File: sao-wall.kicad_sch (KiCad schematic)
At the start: 28 parts, among them J1 Conn_02x03_Odd_Even, J2 Conn_02x03_Odd_Even, J3 Conn_02x03_Odd_Even, J4 Conn_02x03_Odd_Even, J5 Conn_02x03_Odd_Even, J6 Conn_02x03_Odd_Even, J7 Conn_Up, J8 Conn_Down, U1 LM2594M-3.3, U2 LM2594M-3.3, U3 LM2594M-3.3, U4 TCA9535PWR

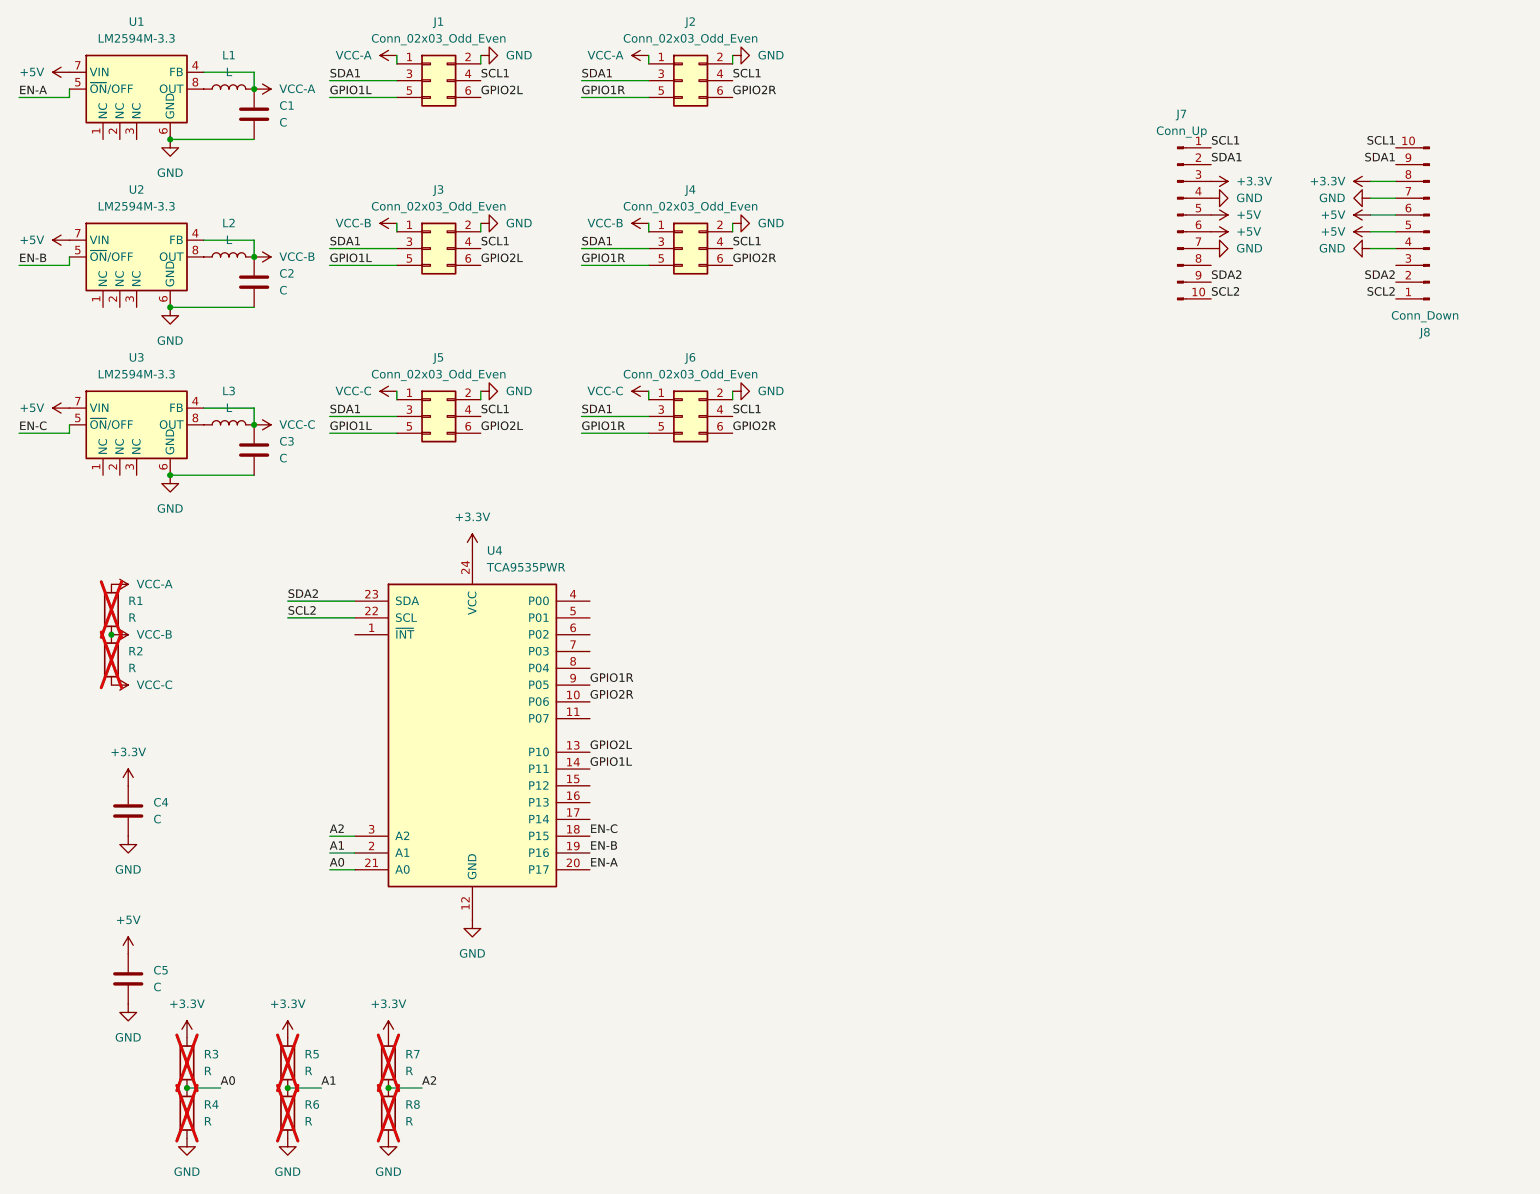
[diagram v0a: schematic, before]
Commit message: Make tile larger, still needs routing
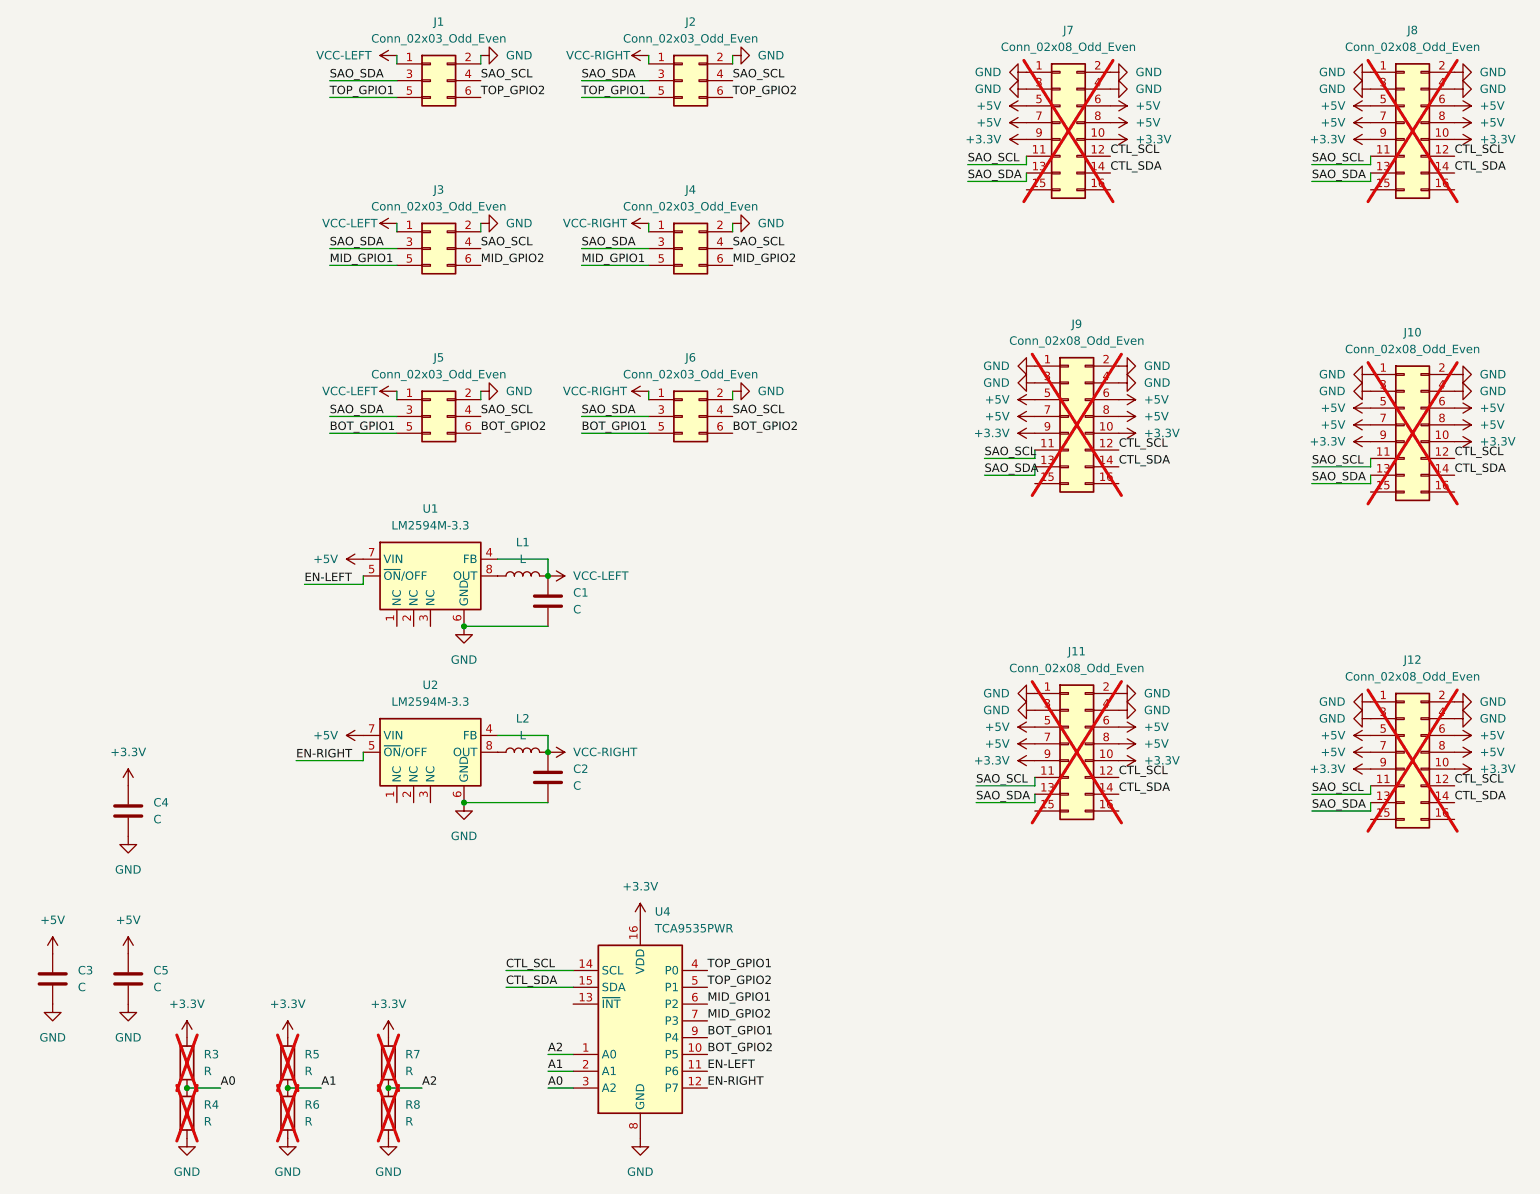
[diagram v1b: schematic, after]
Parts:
- removed J7: Conn_Up, Connector_PinSocket_2.54mm:PinSocket_1x10_P2.54mm_Horizontal, symbol Connector:Conn_01x10_Pin
- removed J8: Conn_Down, Connector_PinSocket_2.54mm:PinSocket_1x10_P2.54mm_Horizontal, symbol Connector:Conn_01x10_Pin
- removed L3: L, Inductor_SMD:L_0603_1608Metric, symbol Device:L
- removed R1, R2: R, Resistor_SMD:R_0603_1608Metric, symbol Device:R
- removed U3: LM2594M-3.3, Package_SO:SOIC-8_3.9x4.9mm_P1.27mm, symbol Regulator_Switching:LM2594M-3.3
- added J10, J11, J12, J7, J8, J9: Conn_02x08_Odd_Even, Connector_PinHeader_2.00mm:PinHeader_2x08_P2.00mm_Vertical, symbol Connector_Generic:Conn_02x08_Odd_Even
- U4: symbol Interface_Expansion:TCA9535PWR -> Interface_Expansion:TCA9534
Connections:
- net +3.3V: now also U4.16 (VDD), J10.10 (Pin_10), J10.9 (Pin_9), J11.10 (Pin_10), J11.9 (Pin_9), J12.10 (Pin_10), J12.9 (Pin_9), J7.10 (Pin_10), J7.9 (Pin_9), J8.10 (Pin_10), J8.9 (Pin_9), J9.10 (Pin_10), J9.9 (Pin_9); no longer U4.24 (VCC)
- net +5V: now also C3.1, J10.5 (Pin_5), J10.6 (Pin_6), J10.7 (Pin_7), J10.8 (Pin_8), J11.5 (Pin_5), J11.6 (Pin_6), J11.7 (Pin_7), J11.8 (Pin_8), J12.5 (Pin_5), J12.6 (Pin_6), J12.7 (Pin_7), J12.8 (Pin_8), J7.5 (Pin_5), J7.6 (Pin_6), J7.7 (Pin_7), J7.8 (Pin_8), J8.5 (Pin_5), J8.6 (Pin_6), J8.7 (Pin_7), J8.8 (Pin_8), J9.5 (Pin_5), J9.6 (Pin_6), J9.7 (Pin_7), J9.8 (Pin_8)
- net A0: now also U4.3 (A2); no longer U4.21 (A0)
- net A2: now also U4.1 (A0); no longer U4.3 (A2)
- net GND: now also U4.8 (GND), J10.1 (Pin_1), J10.2 (Pin_2), J10.3 (Pin_3), J10.4 (Pin_4), J11.1 (Pin_1), J11.2 (Pin_2), J11.3 (Pin_3), J11.4 (Pin_4), J12.1 (Pin_1), J12.2 (Pin_2), J12.3 (Pin_3), J12.4 (Pin_4), J7.1 (Pin_1), J7.2 (Pin_2), J7.3 (Pin_3), J7.4 (Pin_4), J8.1 (Pin_1), J8.2 (Pin_2), J8.3 (Pin_3), J8.4 (Pin_4), J9.1 (Pin_1), J9.2 (Pin_2), J9.3 (Pin_3), J9.4 (Pin_4); no longer U4.12 (GND)
- net EN-LEFT: now reaches U4.11 (P6)
- net EN-LEFT: now also U1.5 (~{ON}/OFF)
- net CTL_SDA: now reaches U4.15 (SDA)
- net CTL_SDA: now also J10.14 (Pin_14), J11.14 (Pin_14), J12.14 (Pin_14), J7.14 (Pin_14), J8.14 (Pin_14), J9.14 (Pin_14)
- net TOP_GPIO1: now reaches U4.4 (P0)
- net TOP_GPIO1: now also J1.5 (Pin_5), J2.5 (Pin_5)
- net TOP_GPIO2: now reaches U4.5 (P1)
- net TOP_GPIO2: now also J1.6 (Pin_6), J2.6 (Pin_6)
- net MID_GPIO1: now reaches U4.6 (P2)
- net MID_GPIO1: now also J3.5 (Pin_5), J4.5 (Pin_5)
- net MID_GPIO2: now reaches U4.7 (P3)
- net MID_GPIO2: now also J3.6 (Pin_6), J4.6 (Pin_6)
- removed net EN-A: U1.5 (~{ON}/OFF), U4.20 (P17)
- net EN-B renamed EN-RIGHT
- net EN-RIGHT: now also U4.12 (P7); no longer U4.19 (P16)
- removed net EN-C: U4.18 (P15)
- removed net GPIO1L: J1.5 (Pin_5), J3.5 (Pin_5), J5.5 (Pin_5), U4.14 (P11)
- net GPIO1R renamed BOT_GPIO1
- net BOT_GPIO1: now also J5.5 (Pin_5); no longer J2.5 (Pin_5), J4.5 (Pin_5)
- removed net GPIO2L: J1.6 (Pin_6), J3.6 (Pin_6), J5.6 (Pin_6), U4.13 (P10)
- net GPIO2R renamed BOT_GPIO2
- net BOT_GPIO2: now also J5.6 (Pin_6); no longer J2.6 (Pin_6), J4.6 (Pin_6)
- net SCL1 renamed SAO_SCL
- net SAO_SCL: now also J10.11 (Pin_11), J11.11 (Pin_11), J12.11 (Pin_11), J7.11 (Pin_11), J8.11 (Pin_11), J9.11 (Pin_11)
- removed net SCL2: U4.22 (SCL)
- net SDA1 renamed SAO_SDA
- net SAO_SDA: now also J10.13 (Pin_13), J11.13 (Pin_13), J12.13 (Pin_13), J7.13 (Pin_13), J8.13 (Pin_13), J9.13 (Pin_13)
- removed net SDA2: U4.23 (SDA)
- net VCC-A renamed VCC-LEFT
- net VCC-LEFT: now also J3.1 (Pin_1), J5.1 (Pin_1); no longer J2.1 (Pin_1)
- net VCC-B renamed VCC-RIGHT
- net VCC-RIGHT: now also J2.1 (Pin_1), J6.1 (Pin_1); no longer J3.1 (Pin_1)
- removed net VCC-C: C3.1, J5.1 (Pin_1), J6.1 (Pin_1)
- new net CTL_SCL: J10.12 (Pin_12), J11.12 (Pin_12), J12.12 (Pin_12), J7.12 (Pin_12), J8.12 (Pin_12), J9.12 (Pin_12), U4.14 (SCL)
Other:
- moved on the sheet: C1, L1, U1
